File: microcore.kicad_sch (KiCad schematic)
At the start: 5 parts, among them J1 TE_776231-1, J8 USB_B_Mini, M1 Module:mega-mcu100/0.3, M2 Module-power_12and5V-0.3, M3 Module-vr-max9924-0.3

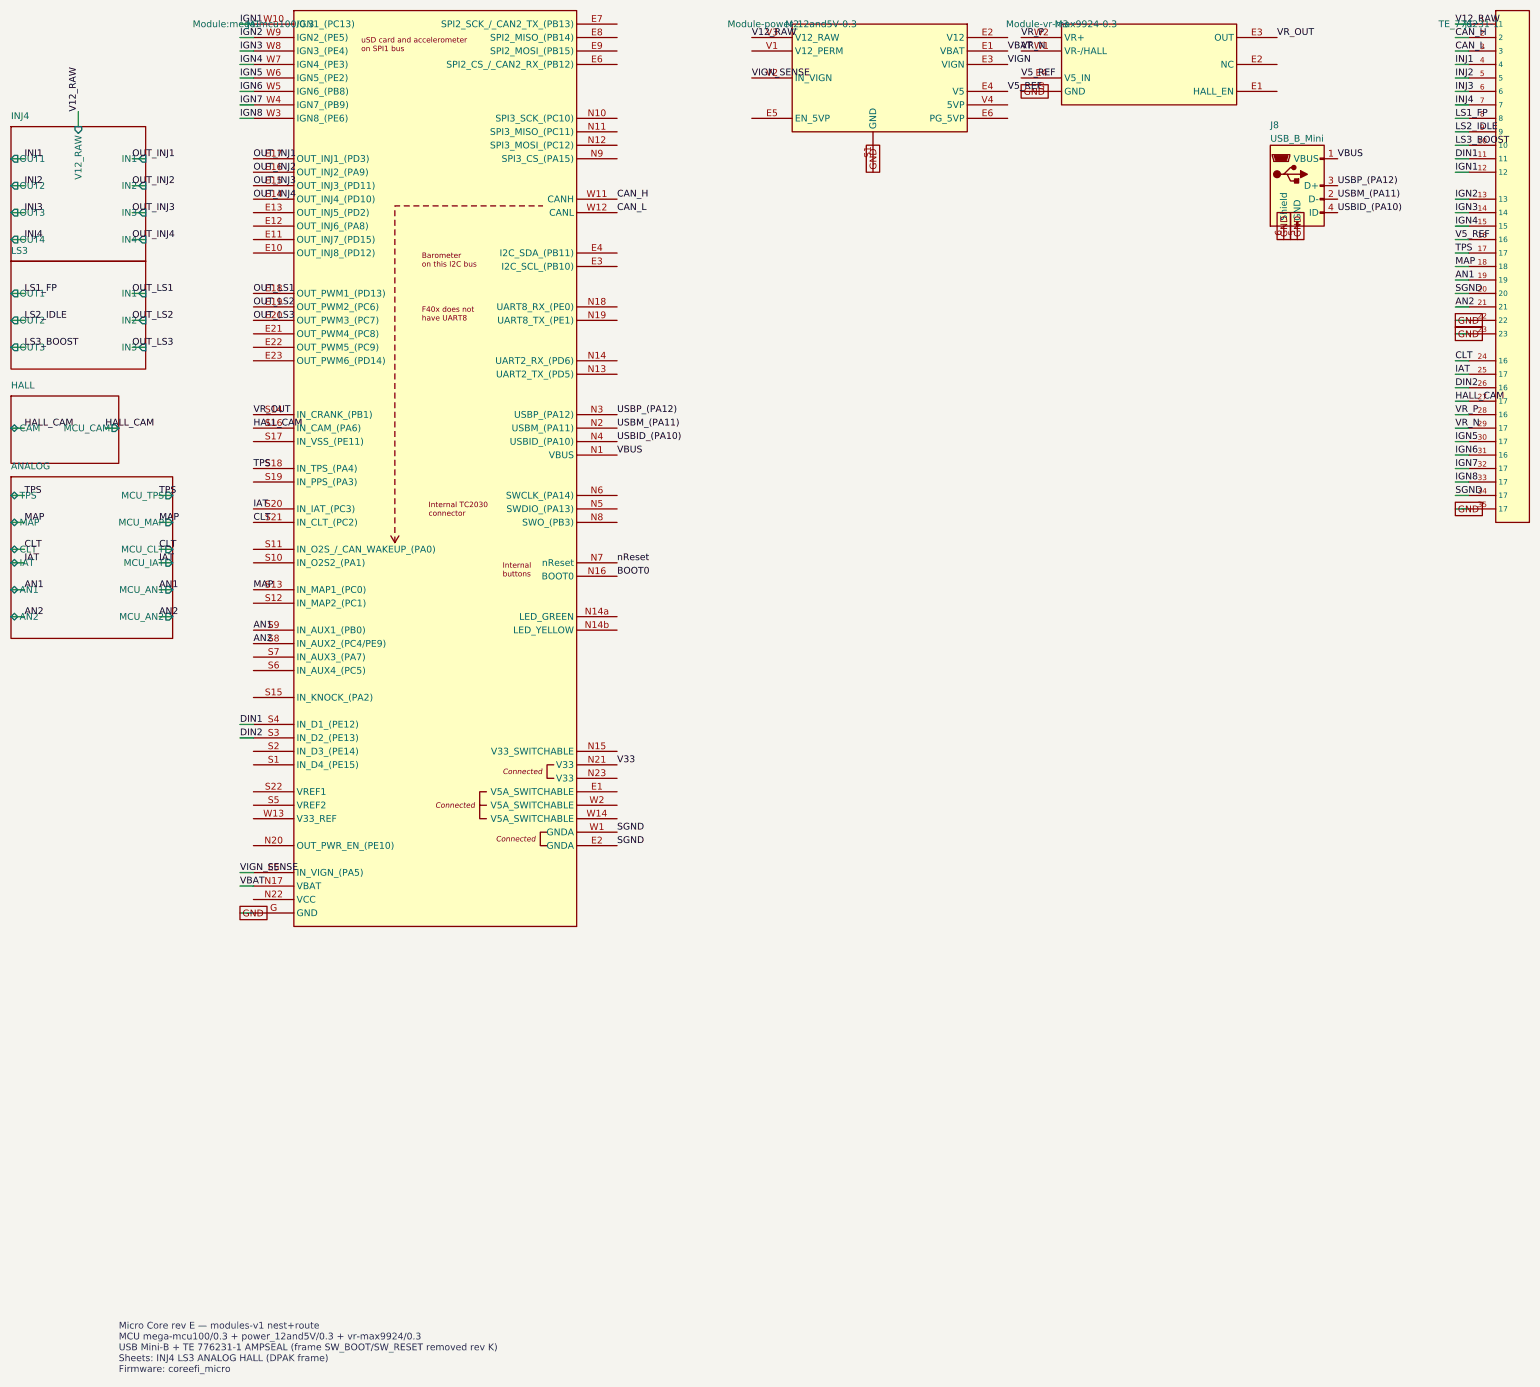
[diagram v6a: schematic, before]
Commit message: Rev n: F407 on mega-mcu100 and drop LS FETs
Swap module U105 from STM32F429VIT6 (C92002) to STM32F407VGT6
(LCSC C12345) in bom_replace_microcore-n.csv. Keep mega-mcu100/0.3.

Remove Q5-Q7 and gate R5-R7 from the LS3 sheet and the PCB, including
their tracks and vias. AMPSEAL pins 8/9/10 are reserved / NC.

Co-authored-by: Quintin <quintinbannink42@users.noreply.github.com>
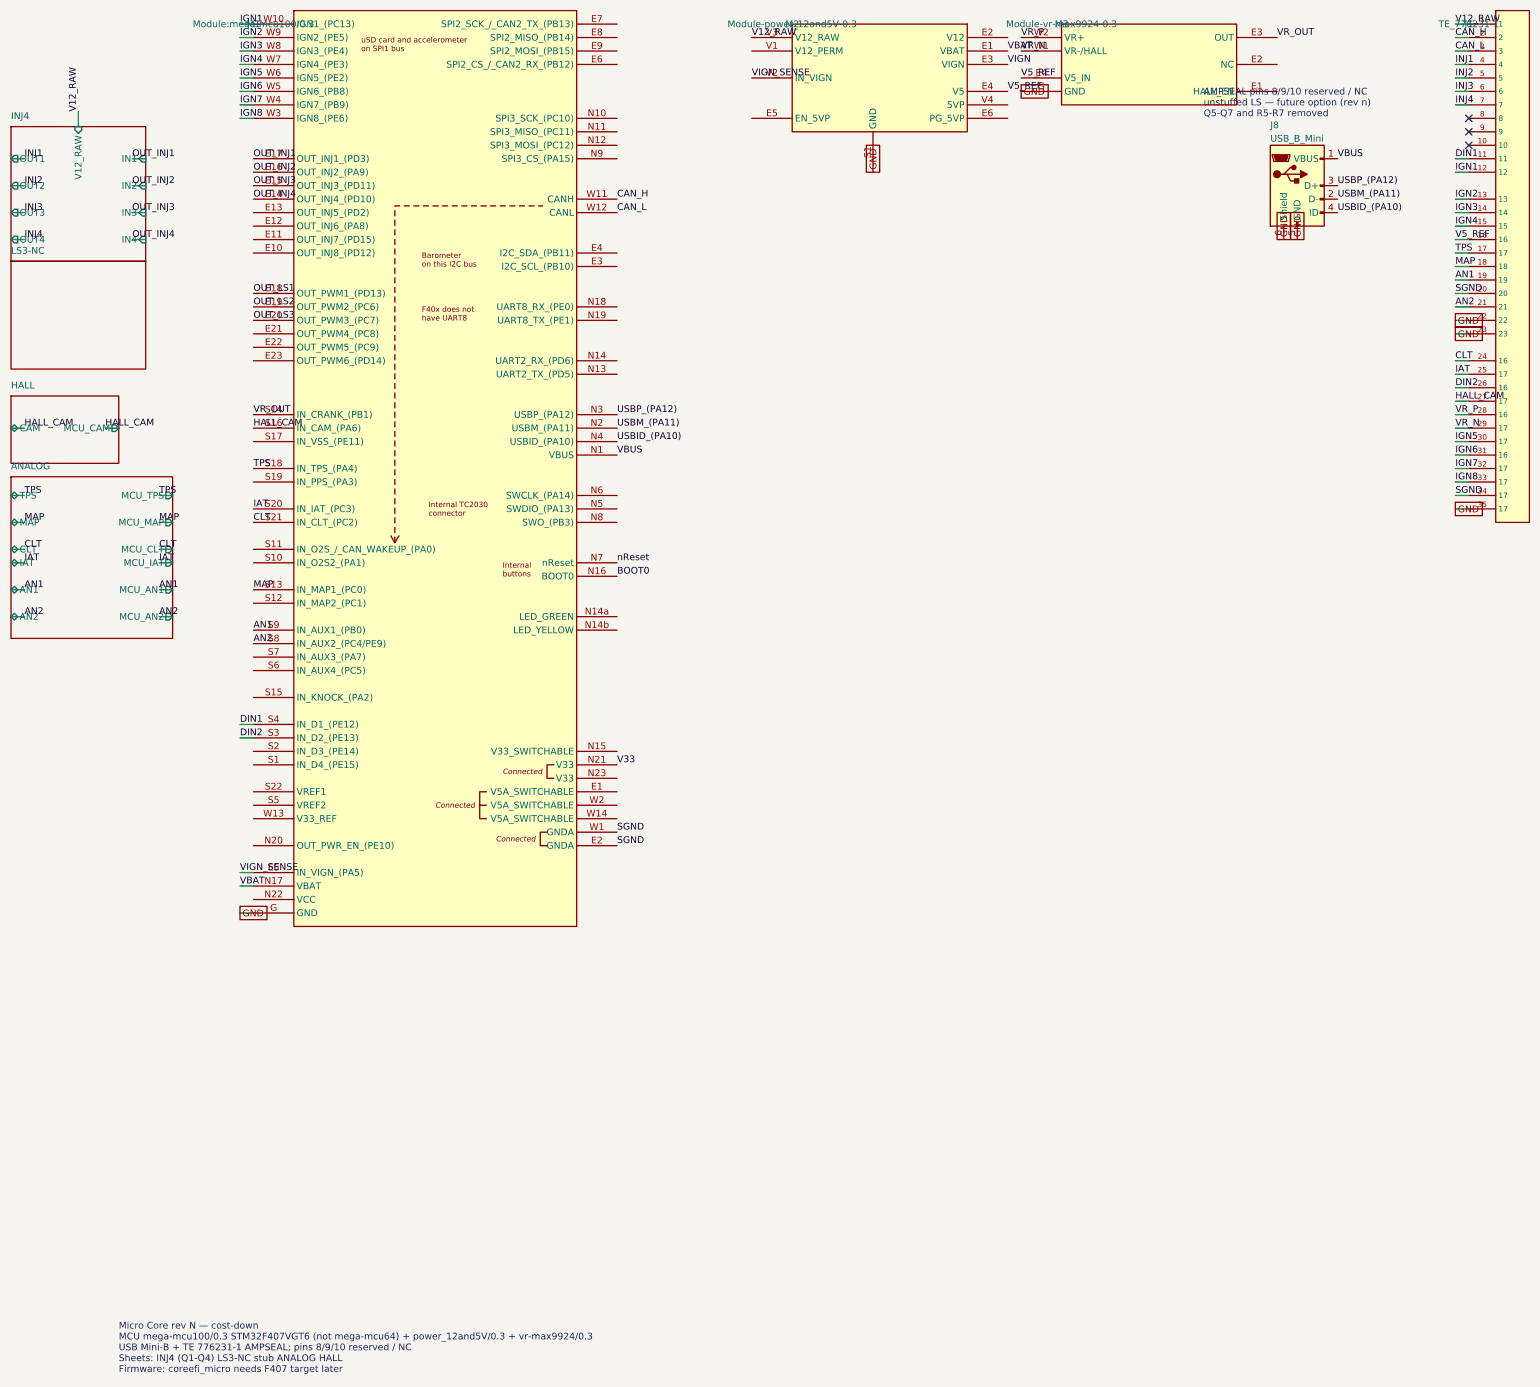
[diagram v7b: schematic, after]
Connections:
- net LS1_FP: no longer names the net of J1.8
- net LS2_IDLE: no longer names the net of J1.9
- net LS3_BOOST: no longer names the net of J1.10
- no-connect marks 0 -> 3
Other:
- sheet LS3 renamed LS3-NC
- sheet LS3-NC ports: added none; removed IN1, IN2, IN3, OUT1, OUT2, OUT3
- note added: "AMPSEAL pins 8/9/10 reserved / NC unstuffed LS — future option (rev n) Q5-Q7 and R5-R7 removed"
- note added: "Micro Core rev N — cost-down MCU mega-mcu100/0.3 STM32F407VGT6 (not mega-mcu64) + power_12and5V/0.3 + vr-max9924/0.3 USB Mini-B + TE 776231-1 AMPSEAL; pins 8/9/10 reserved / NC Sheets: INJ4 (Q1-Q4) LS3-NC stub ANALOG HALL Firmware: coreefi_micro needs F407 target later"
- note removed: "Micro Core rev E — modules-v1 nest+route MCU mega-mcu100/0.3 + power_12and5V/0.3 + vr-max9924/0.3 USB Mini-B + TE 776231-1 AMPSEAL (frame SW_BOOT/SW_RESET removed rev K) Sheets: INJ4 LS3 ANALOG HALL (DPAK frame) Firmware: coreefi_micro"
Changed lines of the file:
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@@
 	(title_block
 		(title "Micro Core")
-		(date "2026-09-15")
-		(rev "E")
+		(date "2026-09-22")
+		(rev "N")
 		(company "Core EFI")
-		(comment 1 "modules-v1 rev E — nest DPAKs + frame routing + GND pours")
-		(comment 2 "Firmware board: coreefi_micro")
+		(comment 1 "rev n cost-down: F407VGT6 on mega-mcu100; LS Q5-Q7 removed")
+		(comment 2 "Firmware board: coreefi_micro — needs F407 target later; fw not in this repo")
 		(comment 3 "PCB basename: microcore (no dashes/underscores)")
 	)
@@
 			(color 0 0 0 0.0000)
 		)
-		(property "Sheetname" "LS3"
+		(property "Sheetname" "LS3-NC"
 			(at 5.08 68.87 0)
 			(effects
@@
 				(justify left top)
 				(hide yes)
-			)
-		)
-		(pin "OUT1" output
-			(at 5.08 76.2 180)
-			(effects
-				(font
-					(size 1.27 1.27)
-				)
-				(justify left)
-			)
-		)
-		(pin "OUT2" output
-			(at 5.08 81.28 180)
-			(effects
-				(font
-					(size 1.27 1.27)
-				)
-				(justify left)
-			)
-		)
-		(pin "OUT3" output
-			(at 5.08 86.36 180)
-			(effects
-				(font
-					(size 1.27 1.27)
-				)
-				(justify left)
-			)
-		)
-		(pin "IN1" input
-			(at 30.48 76.2 0)
-			(effects
-				(font
-					(size 1.27 1.27)
-				)
-				(justify right)
-			)
-		)
-		(pin "IN2" input
-			(at 30.48 81.28 0)
-			(effects
-				(font
-					(size 1.27 1.27)
-				)
-				(justify right)
-			)
-		)
-		(pin "IN3" input
-			(at 30.48 86.36 0)
-			(effects
-				(font
-					(size 1.27 1.27)
-				)
-				(justify right)
 			)
 		)
@@
 		)
 	)
-	(text "Micro Core rev E — modules-v1 nest+route\nMCU mega-mcu100/0.3 + power_12and5V/0.3 + vr-max9924/0.3\nUSB Mini-B + TE 776231-1 AMPSEAL (frame SW_BOOT/SW_RESET removed rev K)\nSheets: INJ4 LS3 ANALOG HALL (DPAK frame)\nFirmware: coreefi_micro"
+	(text "Micro Core rev N — cost-down\nMCU mega-mcu100/0.3 STM32F407VGT6 (not mega-mcu64) + power_12and5V/0.3 + vr-max9924/0.3\nUSB Mini-B + TE 776231-1 AMPSEAL; pins 8/9/10 reserved / NC\nSheets: INJ4 (Q1-Q4) LS3-NC stub ANALOG HALL\nFirmware: coreefi_micro needs F407 target later"
 		(exclude_from_sim no)
 		(at 25.4 280 0)
@@
 	(wire
 		(pts
-			(xy 280 43.18) (xy 277.46 43.18)
-		)
-		(stroke
-			(width 0)
-			(type default)
-		)
-	)
-	(label "LS1_FP"
-		(at 277.46 43.18 180)
-		(effects
-			(font
-				(size 1.27 1.27)
-			)
-			(justify left bottom)
-		)
-	)
-	(wire
-		(pts
-			(xy 280 45.72) (xy 277.46 45.72)
-		)
-		(stroke
-			(width 0)
-			(type default)
-		)
-	)
-	(label "LS2_IDLE"
-		(at 277.46 45.72 180)
-		(effects
-			(font
-				(size 1.27 1.27)
-			)
-			(justify left bottom)
-		)
-	)
-	(wire
-		(pts
-			(xy 280 48.26) (xy 277.46 48.26)
-		)
-		(stroke
-			(width 0)
-			(type default)
-		)
-	)
-	(label "LS3_BOOST"
-		(at 277.46 48.26 180)
-		(effects
-			(font
-				(size 1.27 1.27)
-			)
-			(justify left bottom)
-		)
-	)
-	(wire
-		(pts
 			(xy 280 53.34) (xy 277.46 53.34)
 		)
@@
 	(wire
 		(pts
-			(xy 5.08 76.2) (xy 7.62 76.2)
-		)
-		(stroke
-			(width 0)
-			(type default)
-		)
-	)
-	(label "LS1_FP"
-		(at 7.62 76.2 0)
-		(effects
-			(font
-				(size 1.27 1.27)
-			)
-			(justify left bottom)
-		)
-	)
-	(wire
-		(pts
-			(xy 5.08 81.28) (xy 7.62 81.28)
-		)
-		(stroke
-			(width 0)
-			(type default)
-		)
-	)
-	(label "LS2_IDLE"
-		(at 7.62 81.28 0)
-		(effects
-			(font
-				(size 1.27 1.27)
-			)
-			(justify left bottom)
-		)
-	)
-	(wire
-		(pts
-			(xy 5.08 86.36) (xy 7.62 86.36)
-		)
-		(stroke
-			(width 0)
-			(type default)
-		)
-	)
-	(label "LS3_BOOST"
-		(at 7.62 86.36 0)
-		(effects
-			(font
-				(size 1.27 1.27)
-			)
-			(justify left bottom)
-		)
-	)
-	(wire
-		(pts
-			(xy 30.48 76.2) (xy 27.94 76.2)
-		)
-		(stroke
-			(width 0)
-			(type default)
-		)
-	)
-	(label "OUT_LS1"
-		(at 27.94 76.2 180)
-		(effects
-			(font
-				(size 1.27 1.27)
-			)
-			(justify left bottom)
-		)
-	)
-	(wire
-		(pts
-			(xy 30.48 81.28) (xy 27.94 81.28)
-		)
-		(stroke
-			(width 0)
-			(type default)
-		)
-	)
-	(label "OUT_LS2"
-		(at 27.94 81.28 180)
-		(effects
-			(font
-				(size 1.27 1.27)
-			)
-			(justify left bottom)
-		)
-	)
-	(wire
-		(pts
-			(xy 30.48 86.36) (xy 27.94 86.36)
-		)
-		(stroke
-			(width 0)
-			(type default)
-		)
-	)
-	(label "OUT_LS3"
-		(at 27.94 86.36 180)
-		(effects
-			(font
-				(size 1.27 1.27)
-			)
-			(justify left bottom)
-		)
-	)
-	(wire
-		(pts
 			(xy 5.08 114.3) (xy 7.62 114.3)
 		)
@@
 		(effects
 			(font
+				(size 1.27 1.27)
+			)
+			(justify left bottom)
+		)
+	)
+	(no_connect
+		(at 280 43.18)
+	)
+	(no_connect
+		(at 280 45.72)
+	)
+	(no_connect
+		(at 280 48.26)
+	)
+	(text "AMPSEAL pins 8/9/10 reserved / NC\nunstuffed LS — future option (rev n)\nQ5-Q7 and R5-R7 removed"
+		(exclude_from_sim no)
+		(at 230 43.18 0)
+		(effects
+			(font
